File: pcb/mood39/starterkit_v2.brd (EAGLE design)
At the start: 36 x 36 mm, 22 parts, among them IC1 TINY85, IC2 LP2950

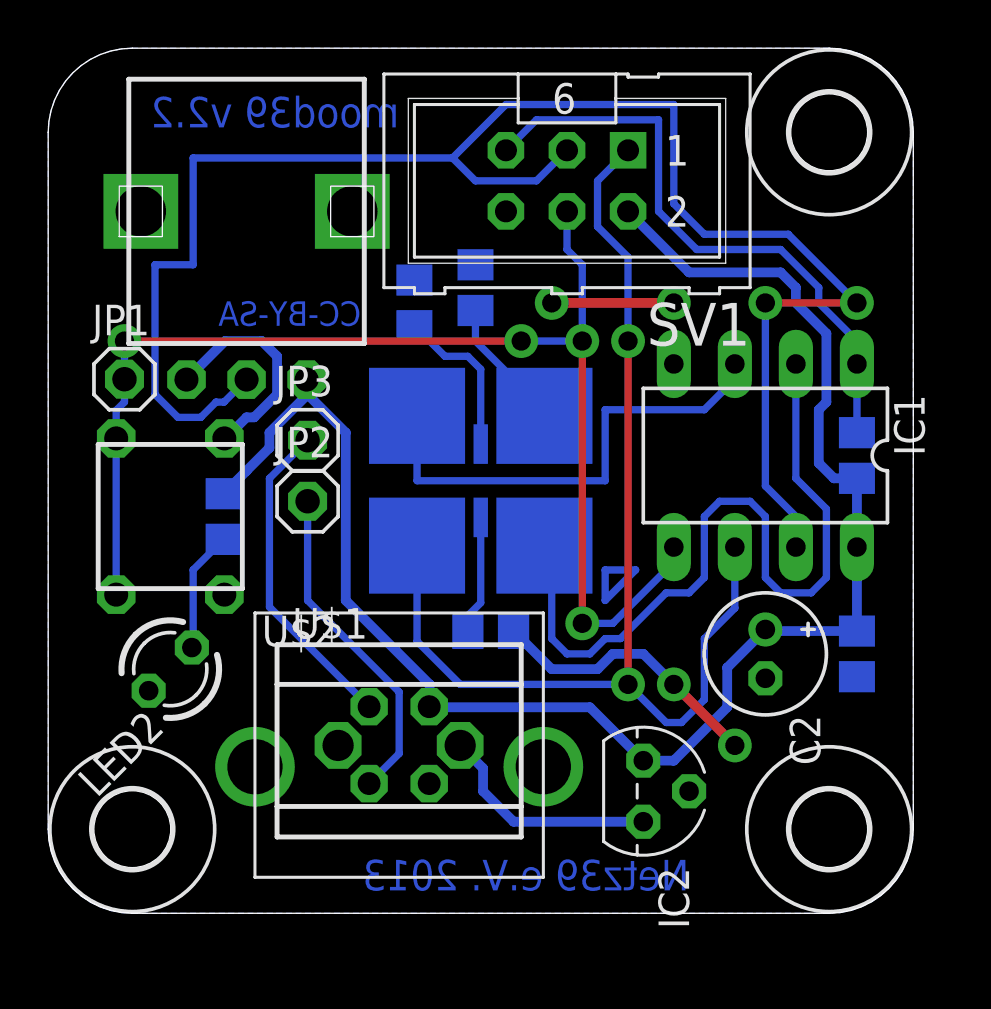
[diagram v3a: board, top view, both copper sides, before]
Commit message: move holes 0.5 mm inward
this is like dangerousprototypes.com does, I always thought the mounting
holes were too near to the edges, see
http://dangerousprototypes.com/docs/Sick_of_Beige_compatible_cases
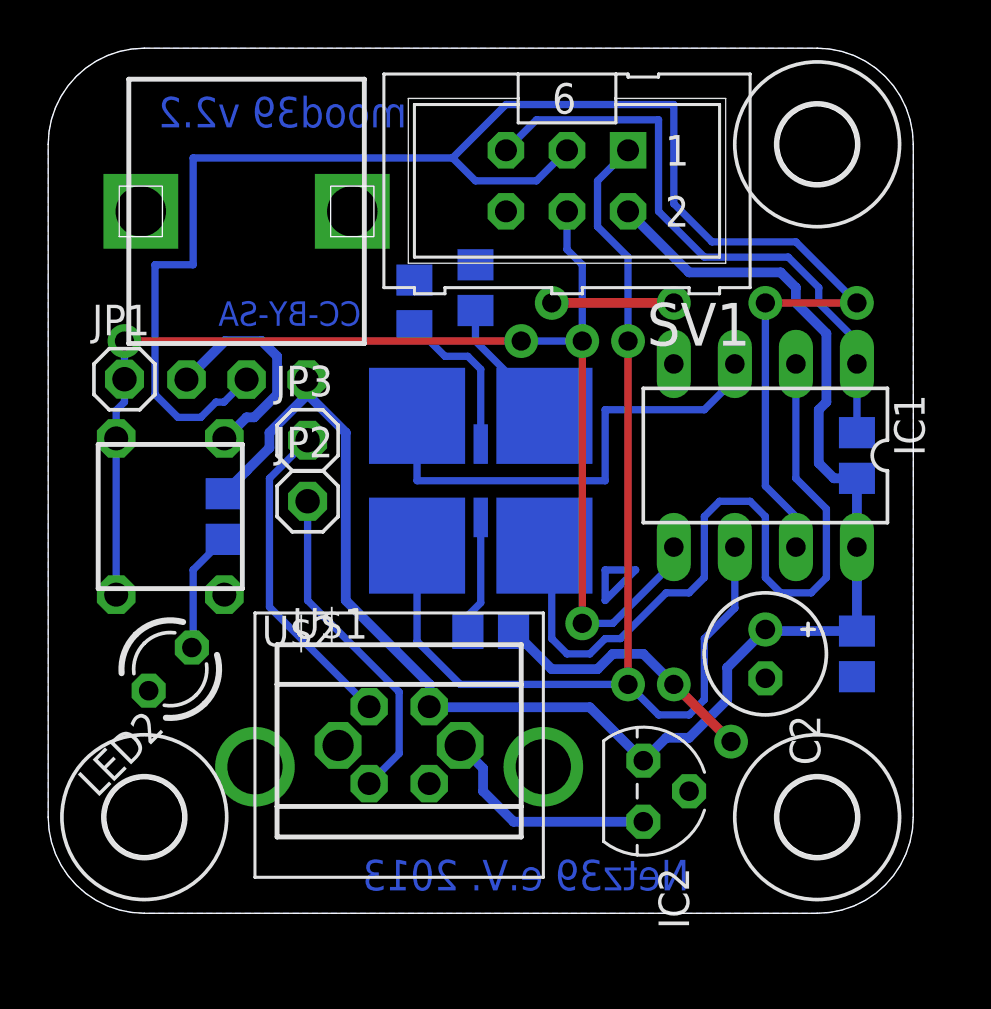
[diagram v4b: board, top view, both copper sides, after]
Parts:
- moved U$4 0.71 mm to (32.0, 32.0)
- moved U$5 0.71 mm to (32.0, 4.00)
- moved U$6 0.71 mm to (4.00, 4.00)
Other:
- outline, holes or cut-outs redrawn
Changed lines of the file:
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@@
 <board>
 <plain>
-<text x="14.605" y="32.7025" size="1.27" layer="16" font="vector" ratio="13" rot="MR0">mood39 v2.2</text>
+<text x="14.9225" y="32.7025" size="1.27" layer="16" font="vector" ratio="13" rot="MR0">mood39 v2.2</text>
 <text x="26.67" y="0.9525" size="1.27" layer="16" font="vector" ratio="13" rot="MR0">Netz39 e.V. 2013</text>
 <text x="13.0175" y="24.4475" size="1.016" layer="16" font="vector" ratio="13" rot="MR0">CC-BY-SA</text>
-<wire x1="3.5" y1="0" x2="32.5" y2="0" width="0" layer="20"/>
-<wire x1="36" y1="3.5" x2="36" y2="32.5" width="0" layer="20"/>
-<wire x1="32.5" y1="36" x2="3.5" y2="36" width="0" layer="20"/>
-<wire x1="0" y1="32.5" x2="0" y2="3.5" width="0" layer="20"/>
-<wire x1="0" y1="32.5" x2="3.5" y2="36" width="0" layer="20" curve="-90"/>
-<wire x1="32.5" y1="36" x2="36" y2="32.5" width="0" layer="20" curve="-90"/>
-<wire x1="36" y1="3.5" x2="32.5" y2="0" width="0" layer="20" curve="-90"/>
-<wire x1="3.5" y1="0" x2="0" y2="3.5" width="0" layer="20" curve="-90"/>
+<wire x1="4" y1="0" x2="32" y2="0" width="0" layer="20"/>
+<wire x1="36" y1="4" x2="36" y2="32" width="0" layer="20"/>
+<wire x1="32" y1="36" x2="4" y2="36" width="0" layer="20"/>
+<wire x1="0" y1="32" x2="0" y2="4" width="0" layer="20"/>
 <rectangle x1="9.8425" y1="0.9525" x2="26.67" y2="1.905" layer="42"/>
-<rectangle x1="2.8575" y1="32.7025" x2="14.605" y2="33.655" layer="42"/>
+<rectangle x1="2.8575" y1="32.7025" x2="14.9225" y2="33.655" layer="42"/>
+<wire x1="4" y1="0" x2="0" y2="4" width="0" layer="20" curve="-90"/>
+<wire x1="0" y1="32" x2="4" y2="36" width="0" layer="20" curve="-90"/>
+<wire x1="32" y1="36" x2="36" y2="32" width="0" layer="20" curve="-90"/>
+<wire x1="36" y1="4" x2="32" y2="0" width="0" layer="20" curve="-90"/>
 </plain>
 <attributes>
@@
 </class>
 </classes>
-<designrules name="starterkit_v2">
+<designrules name="starterkit_v2 *">
 <description language="de">&lt;b&gt;EAGLE Design Rules&lt;/b&gt;
 &lt;p&gt;
@@
 <attribute name="REICHELT" value="USB BG" x="14.605" y="5.3975" size="1.778" layer="27" display="off"/>
 </element>
-<element name="U$4" library="holes" package="3,2" value="" x="32.5" y="32.5"/>
-<element name="U$5" library="holes" package="3,2" value="" x="32.5" y="3.5"/>
-<element name="U$6" library="holes" package="3,2" value="" x="3.5" y="3.5"/>
+<element name="U$4" library="holes" package="3,2" value="" x="32" y="32"/>
+<element name="U$5" library="holes" package="3,2" value="" x="32" y="4"/>
+<element name="U$6" library="holes" package="3,2" value="" x="4" y="4"/>
 </elements>
 <signals>
@@
 <wire x1="28.575" y1="15.24" x2="28.575" y2="12.7" width="0.3048" layer="16"/>
 <wire x1="28.575" y1="12.7" x2="27.305" y2="11.43" width="0.3048" layer="16"/>
-<wire x1="27.305" y1="11.43" x2="27.305" y2="8.89" width="0.3048" layer="16"/>
-<wire x1="27.305" y1="8.89" x2="26.3525" y2="7.9375" width="0.3048" layer="16"/>
-<wire x1="26.3525" y1="7.9375" x2="25.7175" y2="7.9375" width="0.3048" layer="16"/>
-<wire x1="25.7175" y1="7.9375" x2="24.13" y2="9.525" width="0.3048" layer="16"/>
 <wire x1="22.86" y1="30.48" x2="22.86" y2="28.575" width="0.3048" layer="16"/>
 <wire x1="22.86" y1="28.575" x2="24.13" y2="27.305" width="0.3048" layer="16"/>
@@
 <via x="24.13" y="23.8125" extent="1-16" drill="0.8" shape="octagon"/>
 <wire x1="22.86" y1="30.48" x2="24.13" y2="31.75" width="0.3048" layer="16"/>
+<wire x1="27.305" y1="11.43" x2="27.305" y2="8.89" width="0.3048" layer="16"/>
+<wire x1="27.305" y1="8.89" x2="26.67" y2="8.255" width="0.3048" layer="16"/>
+<wire x1="26.67" y1="8.255" x2="25.4" y2="8.255" width="0.3048" layer="16"/>
+<wire x1="25.4" y1="8.255" x2="24.13" y2="9.525" width="0.3048" layer="16"/>
 </signal>
 <signal name="PB3" class="2">
@@
 <contactref element="R5" pad="1"/>
 <via x="26.035" y="9.525" extent="1-16" drill="0.8" shape="octagon"/>
-<via x="28.575" y="6.985" extent="1-16" drill="0.8" shape="octagon"/>
+<via x="28.41625" y="7.14375" extent="1-16" drill="0.8" shape="octagon"/>
 <wire x1="26.035" y1="9.525" x2="24.765" y2="10.795" width="0.4064" layer="16"/>
 <wire x1="24.765" y1="10.795" x2="23.495" y2="10.795" width="0.4064" layer="16"/>
@@
 <wire x1="22.86" y1="10.16" x2="20.9525" y2="10.16" width="0.4064" layer="16"/>
 <wire x1="20.9525" y1="10.16" x2="19.365" y2="11.7475" width="0.4064" layer="16"/>
-<wire x1="26.035" y1="9.525" x2="28.575" y2="6.985" width="0.4064" layer="1"/>
+<wire x1="26.035" y1="9.525" x2="28.41625" y2="7.14375" width="0.4064" layer="1"/>
 <wire x1="9.525" y1="21.59" x2="9.525" y2="23.1775" width="0.4064" layer="16"/>
 <wire x1="7.3575" y1="23.8125" x2="5.755" y2="22.21" width="0.4064" layer="16"/>
@@
 <via x="20.955" y="25.4" extent="1-16" drill="0.8" shape="octagon"/>
 <wire x1="20.955" y1="25.4" x2="26.035" y2="25.4" width="0.4064" layer="1"/>
-<polygon width="0.4064" layer="16" thermals="no">
-<vertex x="3.5" y="0"/>
-<vertex x="32.5" y="0" curve="90"/>
-<vertex x="36" y="3.5"/>
-<vertex x="36" y="32.5" curve="90"/>
-<vertex x="32.5" y="36"/>
-<vertex x="3.5" y="36" curve="90"/>
-<vertex x="0" y="32.5"/>
-<vertex x="0" y="3.5" curve="90"/>
-</polygon>
 <wire x1="7.3575" y1="23.8125" x2="8.89" y2="23.8125" width="0.4064" layer="16"/>
 <wire x1="9.525" y1="23.1775" x2="8.89" y2="23.8125" width="0.4064" layer="16"/>
+<polygon width="0.4064" layer="16">
+<vertex x="0" y="32" curve="-90"/>
+<vertex x="4" y="36"/>
+<vertex x="32" y="36" curve="-90"/>
+<vertex x="36" y="32"/>
+<vertex x="36" y="4" curve="-90"/>
+<vertex x="32" y="0"/>
+<vertex x="4" y="0" curve="-90"/>
+<vertex x="0" y="4"/>
+</polygon>
 </signal>
 <signal name="VCC" class="1">
@@
 <wire x1="15.875" y1="9.525" x2="15.875" y2="8.6175" width="0.4064" layer="16"/>
 <wire x1="15.875" y1="8.6175" x2="15.855" y2="8.5975" width="0.4064" layer="16"/>
-<wire x1="24.765" y1="6.35" x2="26.035" y2="6.35" width="0.4064" layer="16"/>
-<wire x1="26.035" y1="6.35" x2="28.2575" y2="8.5725" width="0.4064" layer="16"/>
-<wire x1="28.2575" y1="8.5725" x2="28.2575" y2="10.2235" width="0.4064" layer="16"/>
 <wire x1="28.2575" y1="10.2235" x2="29.845" y2="11.811" width="0.4064" layer="16"/>
 <wire x1="15.88" y1="8.5725" x2="22.5425" y2="8.5725" width="0.4064" layer="16"/>
@@
 <wire x1="8.255" y1="18.415" x2="8.255" y2="18.4125" width="0.4064" layer="16"/>
 <wire x1="8.255" y1="18.4125" x2="7.3025" y2="17.46" width="0.4064" layer="16"/>
+<wire x1="28.2575" y1="10.2235" x2="28.2575" y2="8.89" width="0.4064" layer="16"/>
+<wire x1="28.2575" y1="8.89" x2="26.67" y2="7.3025" width="0.4064" layer="16"/>
+<wire x1="26.67" y1="7.3025" x2="25.7175" y2="7.3025" width="0.4064" layer="16"/>
+<wire x1="25.7175" y1="7.3025" x2="24.765" y2="6.35" width="0.4064" layer="16"/>
 </signal>
 <signal name="N$5" class="2">
@@
 <wire x1="17.78" y1="30.48" x2="16.8275" y2="31.4325" width="0.3048" layer="16"/>
 <wire x1="20.32" y1="30.48" x2="21.59" y2="31.75" width="0.3048" layer="16"/>
-<wire x1="30.7975" y1="28.2575" x2="27.305" y2="28.2575" width="0.3048" layer="16"/>
-<wire x1="27.305" y1="28.2575" x2="26.035" y2="29.5275" width="0.3048" layer="16"/>
+<wire x1="27.6225" y1="27.94" x2="26.035" y2="29.5275" width="0.3048" layer="16"/>
 <wire x1="26.035" y1="29.5275" x2="26.035" y2="33.655" width="0.3048" layer="16"/>
 <wire x1="26.035" y1="33.655" x2="19.05" y2="33.655" width="0.3048" layer="16"/>
-<wire x1="33.655" y1="25.4" x2="30.7975" y2="28.2575" width="0.3048" layer="16"/>
 <wire x1="5.3975" y1="20.6375" x2="6.35" y2="20.6375" width="0.3048" layer="16"/>
 <wire x1="6.35" y1="20.6375" x2="6.985" y2="21.2725" width="0.3048" layer="16"/>
 <wire x1="6.985" y1="21.2725" x2="7.3175" y2="21.2725" width="0.3048" layer="16"/>
+<wire x1="27.6225" y1="27.94" x2="31.115" y2="27.94" width="0.3048" layer="16"/>
+<wire x1="31.115" y1="27.94" x2="33.655" y2="25.4" width="0.3048" layer="16"/>
 </signal>
 <signal name="MOSI" class="2">
@@
 <wire x1="20.32" y1="33.02" x2="25.4" y2="33.02" width="0.3048" layer="16"/>
 <wire x1="25.4" y1="33.02" x2="25.4" y2="29.21" width="0.3048" layer="16"/>
-<wire x1="25.4" y1="29.21" x2="26.9875" y2="27.6225" width="0.3048" layer="16"/>
-<wire x1="26.9875" y1="27.6225" x2="30.48" y2="27.6225" width="0.3048" layer="16"/>
+<wire x1="25.4" y1="29.21" x2="27.305" y2="27.305" width="0.3048" layer="16"/>
 <wire x1="32.0675" y1="26.035" x2="32.0675" y2="25.4" width="0.3048" layer="16"/>
-<wire x1="30.48" y1="27.6225" x2="32.0675" y2="26.035" width="0.3048" layer="16"/>
+<wire x1="32.0675" y1="26.035" x2="30.7975" y2="27.305" width="0.3048" layer="16"/>
+<wire x1="27.305" y1="27.305" x2="30.7975" y2="27.305" width="0.3048" layer="16"/>
 </signal>
 <signal name="N$8">

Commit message: fix complaints of #11
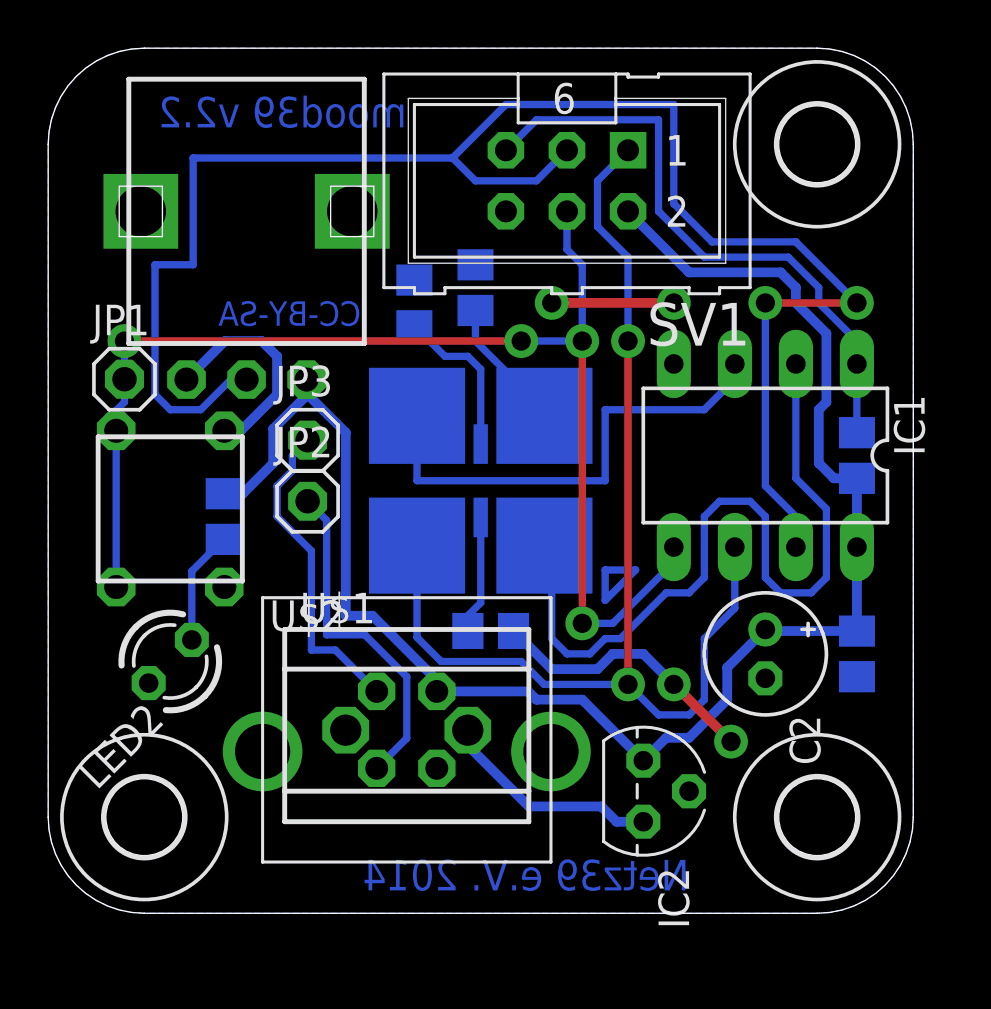
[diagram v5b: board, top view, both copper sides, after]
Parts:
- LED2: value rot lc -> gr lc
- moved U$1 0.71 mm to (14.9, 7.62)
- moved U$2 0.71 mm to (14.9, 6.03)
- moved LED2 0.32 mm to (5.08, 10.5)
- moved S1 0.32 mm to (5.08, 16.8)
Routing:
- net VCC: track 67.6 -> 68.2 mm
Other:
- board text added: "Netz39 e.V. 2014"
- board text removed: "Netz39 e.V. 2013"

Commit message: add via for cnc reference and replace mount pads
Furthermore bump version to v2.3 because we already etched v2.2 and
changed the board afterwards so e.g. milling some v2.2 is not possible
with current master anymore. There's still no tag for v2.2 but I guess
there just won't be any, maybe a branch must be enough for now.
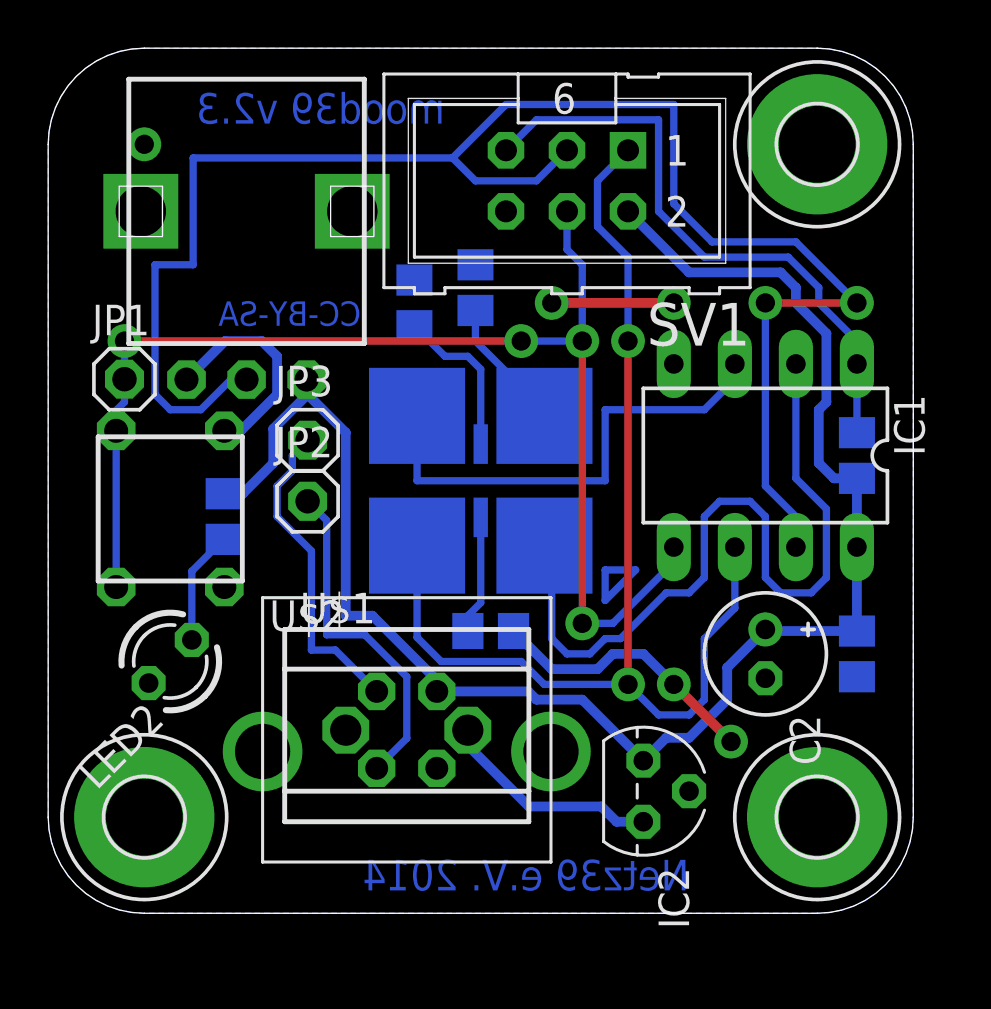
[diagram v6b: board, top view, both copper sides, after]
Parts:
- U$4, U$5, U$6: device holes:3,2 -> holes:3,2-PAD
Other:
- board text added: "mood39 v2.3"
- board text removed: "mood39 v2.2"
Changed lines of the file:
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@@
 <setting verticaltext="up"/>
 </settings>
-<grid distance="25" unitdist="mil" unit="mil" style="dots" multiple="1" display="yes" altdistance="12.5" altunitdist="mil" altunit="mil"/>
+<grid distance="6.25" unitdist="mil" unit="mil" style="dots" multiple="1" display="yes" altdistance="25" altunitdist="mil" altunit="mil"/>
 <layers>
 <layer number="1" name="Top" color="4" fill="1" visible="yes" active="yes"/>
@@
 <board>
 <plain>
-<text x="14.9225" y="32.7025" size="1.27" layer="16" font="vector" ratio="13" rot="MR0">mood39 v2.2</text>
+<text x="16.51" y="32.86125" size="1.27" layer="16" font="vector" ratio="13" rot="MR0">mood39 v2.3</text>
 <text x="26.67" y="0.9525" size="1.27" layer="16" font="vector" ratio="13" rot="MR0">Netz39 e.V. 2014</text>
 <text x="13.0175" y="24.4475" size="1.016" layer="16" font="vector" ratio="13" rot="MR0">CC-BY-SA</text>
@@
 <wire x1="32" y1="36" x2="4" y2="36" width="0" layer="20"/>
 <wire x1="0" y1="32" x2="0" y2="4" width="0" layer="20"/>
-<rectangle x1="9.68375" y1="0.9525" x2="26.51125" y2="1.905" layer="42"/>
-<rectangle x1="2.8575" y1="32.7025" x2="14.9225" y2="33.655" layer="42"/>
 <wire x1="4" y1="0" x2="0" y2="4" width="0" layer="20" curve="-90"/>
 <wire x1="0" y1="32" x2="4" y2="36" width="0" layer="20" curve="-90"/>
 <wire x1="32" y1="36" x2="36" y2="32" width="0" layer="20" curve="-90"/>
 <wire x1="36" y1="4" x2="32" y2="0" width="0" layer="20" curve="-90"/>
+<rectangle x1="15.5575" y1="0.9525" x2="26.67" y2="1.905" layer="42"/>
 </plain>
 <attributes>
@@
 <attribute name="REICHELT" value="USB BG" x="14.9225" y="6.0325" size="1.778" layer="27" display="off"/>
 </element>
-<element name="U$4" library="holes" package="3,2" value="" x="32" y="32"/>
-<element name="U$5" library="holes" package="3,2" value="" x="32" y="4"/>
-<element name="U$6" library="holes" package="3,2" value="" x="4" y="4"/>
+<element name="U$4" library="holes" package="3,2-PAD" value="" x="32" y="32"/>
+<element name="U$5" library="holes" package="3,2-PAD" value="" x="32" y="4"/>
+<element name="U$6" library="holes" package="3,2-PAD" value="" x="4" y="4"/>
 </elements>
 <signals>
@@
 <wire x1="24.4475" y1="14.2875" x2="23.1775" y2="14.2875" width="0.3048" layer="16"/>
 </signal>
+<signal name="N$17">
+<via x="4" y="32" extent="1-16" drill="0.8"/>
+</signal>
 </signals>
